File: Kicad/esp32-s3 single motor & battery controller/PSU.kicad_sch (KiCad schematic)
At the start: 67 parts, among them J5 Batt Balance connector, Q1 NMOS, Q2 NMOS, Q3 NMOS, Q4 NMOS, Q5 NMOS, Q6 NMOS, U1 AP2112K-3.3, U3 BQ76905RGRR, U4 BQ24780SRUYR

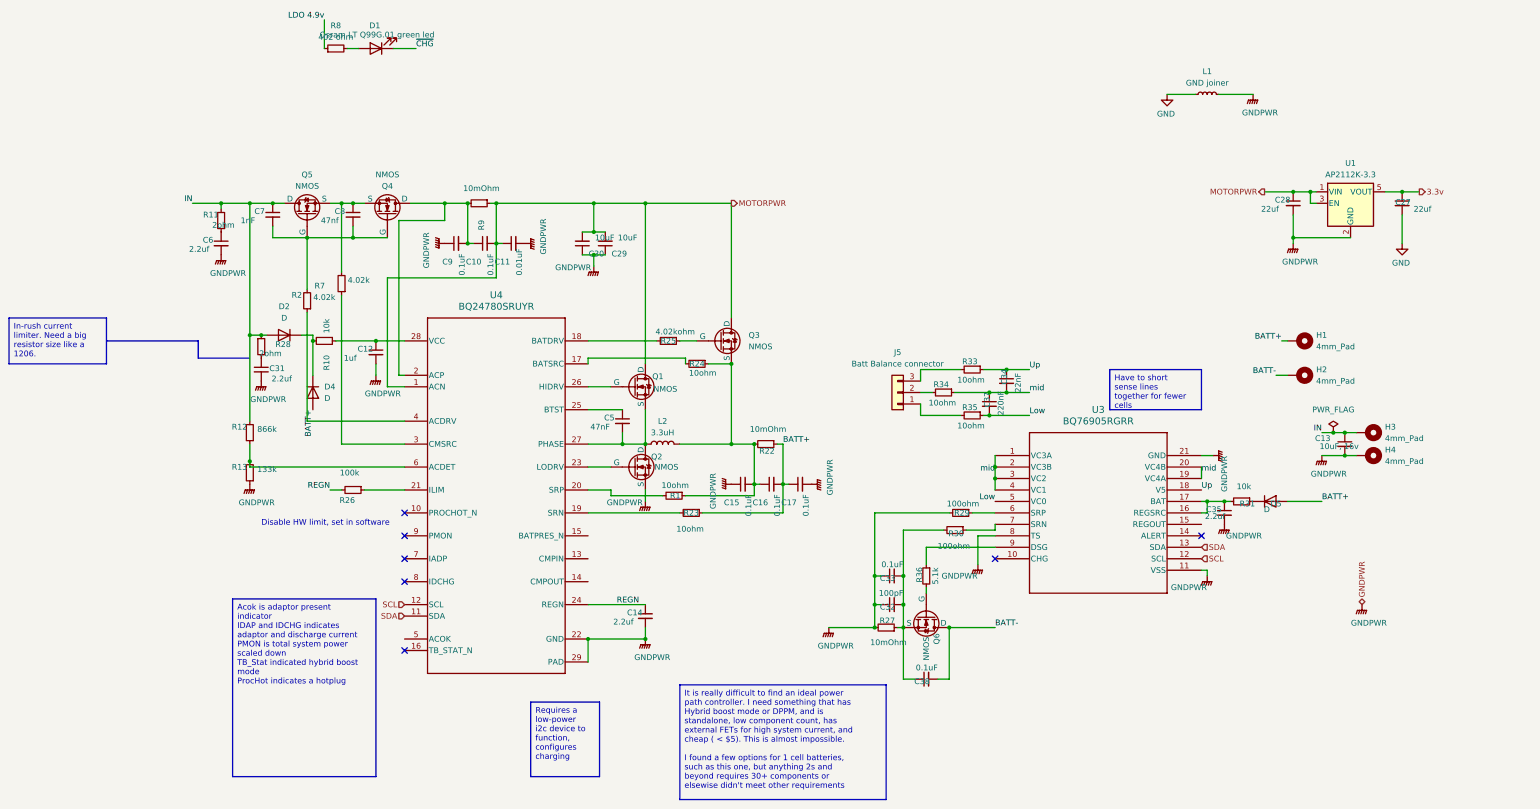
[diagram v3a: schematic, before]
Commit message: Finished schematic routing, Sizing Inductors and mosfets
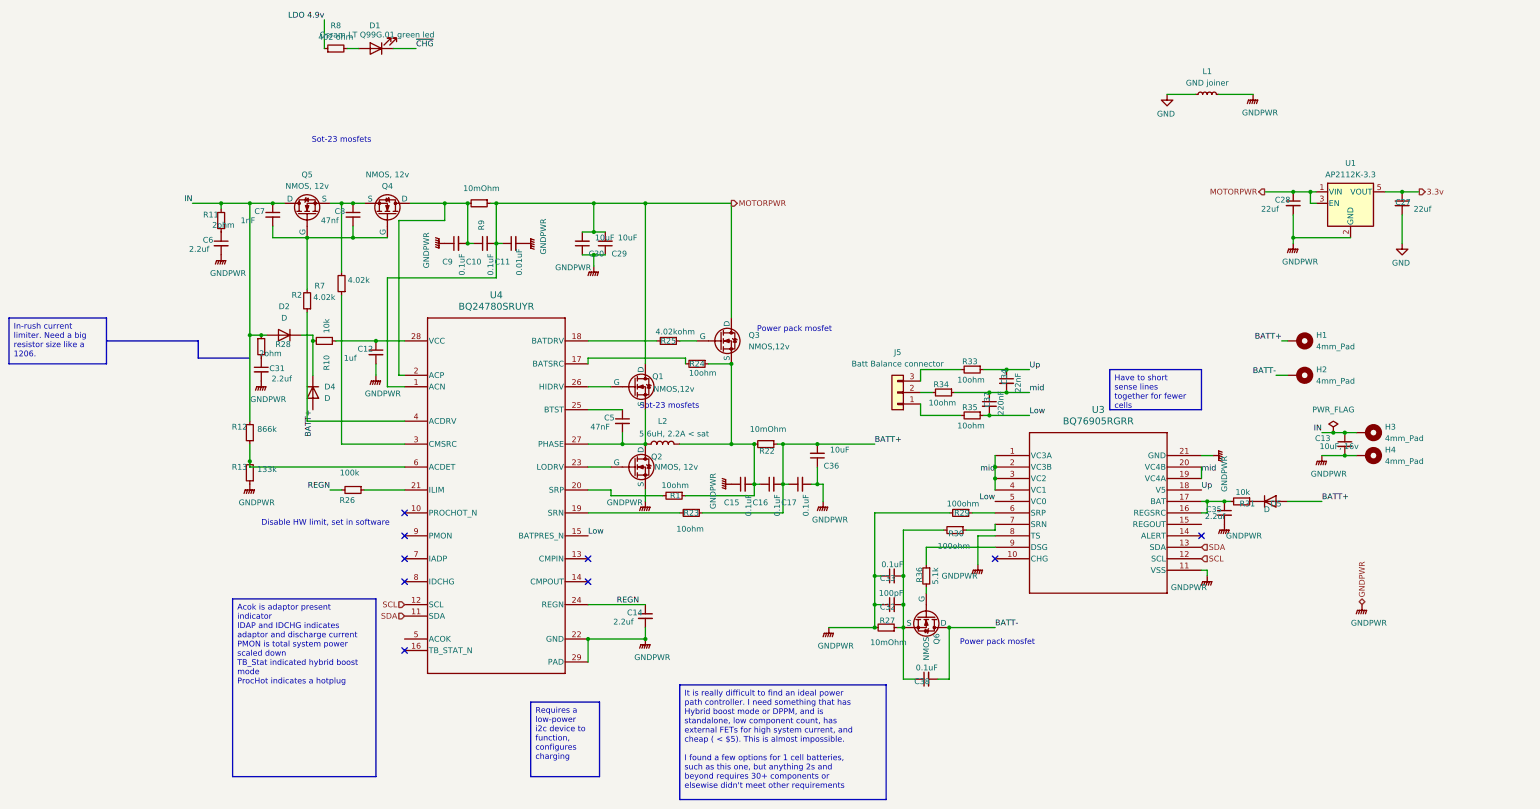
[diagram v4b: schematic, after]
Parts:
- added C36: 10uF, Capacitor_SMD:C_0603_1608Metric, symbol Device:C_Small
- L2: value 3.3uH -> 5.6uH, 2.2A < sat
- Q1, Q3: value NMOS -> NMOS,12v
- Q2, Q4, Q5: value NMOS -> NMOS, 12v
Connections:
- net BATT+: now also C36.2
- net GNDPWR: now also C36.1
- net Low: now also U4.15 (BATPRES_N)
- no-connect marks 7 -> 9
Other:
- note added: "Power pack mosfet"
- note added: "Sot-23 mosfets"
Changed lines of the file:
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@@
 	)
 	(junction
+		(at 144.78 127)
+		(diameter 0)
+		(color 0 0 0 0)
+	)
+	(junction
 		(at 125.73 118.11)
 		(diameter 0)
@@
 	)
 	(junction
+		(at 144.78 118.11)
+		(diameter 0)
+		(color 0 0 0 0)
+	)
+	(junction
 		(at 67.31 64.77)
 		(diameter 0)
@@
 	)
 	(junction
+		(at 137.16 118.11)
+		(diameter 0)
+		(color 0 0 0 0)
+	)
+	(junction
 		(at 261.62 115.57)
 		(diameter 0)
@@
 	)
 	(no_connect
+		(at 93.98 143.51)
+	)
+	(no_connect
 		(at 53.34 148.59)
 	)
 	(no_connect
+		(at 93.98 148.59)
+	)
+	(no_connect
 		(at 184.15 143.51)
 	)
@@
 	(wire
 		(pts
+			(xy 144.78 123.19) (xy 144.78 127)
+		)
+		(stroke
+			(width 0)
+			(type default)
+		)
+	)
+	(wire
+		(pts
 			(xy 233.68 40.64) (xy 241.3 40.64)
 		)
@@
 	(wire
 		(pts
+			(xy 146.05 130.81) (xy 146.05 127)
+		)
+		(stroke
+			(width 0)
+			(type default)
+		)
+	)
+	(wire
+		(pts
 			(xy 93.98 133.35) (xy 114.3 133.35)
 		)
@@
 	(wire
 		(pts
+			(xy 144.78 127) (xy 143.51 127)
+		)
+		(stroke
+			(width 0)
+			(type default)
+		)
+	)
+	(wire
+		(pts
 			(xy 180.34 138.43) (xy 184.15 138.43)
 		)
@@
 	(wire
 		(pts
+			(xy 146.05 127) (xy 144.78 127)
+		)
+		(stroke
+			(width 0)
+			(type default)
+		)
+	)
+	(wire
+		(pts
 			(xy 106.68 110.49) (xy 106.68 118.11)
 		)
@@
 	(wire
 		(pts
+			(xy 144.78 118.11) (xy 157.48 118.11)
+		)
+		(stroke
+			(width 0)
+			(type default)
+		)
+	)
+	(wire
+		(pts
 			(xy 93.98 110.49) (xy 101.6 110.49)
 		)
@@
 	(wire
 		(pts
+			(xy 137.16 118.11) (xy 144.78 118.11)
+		)
+		(stroke
+			(width 0)
+			(type default)
+		)
+	)
+	(wire
+		(pts
 			(xy 261.62 120.65) (xy 264.16 120.65)
 		)
@@
 		)
 	)
+	(text "Sot-23 mosfets"
+		(exclude_from_sim no)
+		(at 39.37 50.8 0)
+		(effects
+			(font
+				(size 1.27 1.27)
+			)
+		)
+	)
+	(text "Sot-23 mosfets"
+		(exclude_from_sim no)
+		(at 112.014 109.728 0)
+		(effects
+			(font
+				(size 1.27 1.27)
+			)
+		)
+	)
 	(text "Disable HW limit, set in software"
 		(exclude_from_sim no)
@@
 		)
 	)
+	(text "Power pack mosfet"
+		(exclude_from_sim no)
+		(at 184.658 162.052 0)
+		(effects
+			(font
+				(size 1.27 1.27)
+			)
+		)
+	)
+	(text "Power pack mosfet"
+		(exclude_from_sim no)
+		(at 139.7 92.71 0)
+		(effects
+			(font
+				(size 1.27 1.27)
+			)
+		)
+	)
 	(label "BATT-"
 		(at 246.38 102.87 180)
@@
 		)
 	)
+	(label "Low"
+		(at 93.98 138.43 0)
+		(fields_autoplaced yes)
+		(effects
+			(font
+				(size 1.27 1.27)
+			)
+			(justify left bottom)
+		)
+	)
 	(label "REGN"
 		(at 36.83 128.27 180)
@@
 	)
 	(label "BATT+"
-		(at 137.16 118.11 0)
+		(at 157.48 118.11 0)
 		(fields_autoplaced yes)
 		(effects
@@
 	)
 	(symbol
+		(lib_id "Device:C_Small")
+		(at 144.78 120.65 180)
+		(unit 1)
+		(exclude_from_sim no)
+		(in_bom yes)
+		(on_board yes)
+		(dnp no)
+		(property "Reference" "C36"
+			(at 149.606 122.936 0)
+			(effects
+				(font
+					(size 1.27 1.27)
+				)
+				(justify left)
+			)
+		)
+		(property "Value" "10uF"
+			(at 151.892 119.38 0)
+			(effects
+				(font
+					(size 1.27 1.27)
+				)
+				(justify left)
+			)
+		)
+		(property "Footprint" "Capacitor_SMD:C_0603_1608Metric"
+			(at 144.78 120.65 0)
+			(effects
+				(font
+					(size 1.27 1.27)
+				)
+				(hide yes)
+			)
+		)
+		(property "Datasheet" "~"
+			(at 144.78 120.65 0)
+			(effects
+				(font
+					(size 1.27 1.27)
+				)
+				(hide yes)
+			)
+		)
+		(property "Description" "Unpolarized capacitor, small symbol"
+			(at 144.78 120.65 0)
+			(effects
+				(font
+					(size 1.27 1.27)
+				)
+				(hide yes)
+			)
+		)
+		(pin "1"
+		)
+		(pin "2"
+		)
+		(instances
+			(project "esp32-s3 single motor & battery controller"
+				(path "/eb3f183d-8bb1-43a5-a363-092ed67891e3/a57a0b4f-e246-497c-8d94-688647d8fd03"
+					(reference "C36")
+					(unit 1)
+				)
+			)
+		)
+	)
+	(symbol
 		(lib_id "power:GNDPWR")
 		(at 106.68 130.81 0)
@@
 			)
 		)
-		(property "Value" "NMOS"
+		(property "Value" "NMOS, 12v"
 			(at 49.53 58.42 90)
 			(effects
@@
 		)
 		(property "Value" "10k"
-			(at 239.268 127.508 90)
+			(at 239.014 128.778 90)
 			(effects
 				(font
@@
 		(on_board yes)
 		(dnp no)
-		(fields_autoplaced yes)
 		(property "Reference" "L2"
 			(at 110.49 113.03 90)
@@
 			)
 		)
-		(property "Value" "3.3uH"
-			(at 110.49 115.57 90)
+		(property "Value" "5.6uH, 2.2A < sat"
+			(at 113.03 115.824 90)
 			(effects
 				(font
@@
 			)
 		)
-		(property "Value" "NMOS"
+		(property "Value" "NMOS, 12v"
 			(at 108.712 123.19 0)
 			(effects
@@
 			)
 		)
-		(property "Value" "NMOS"
+		(property "Value" "NMOS,12v"
 			(at 129.54 96.5199 0)
 			(effects
@@
 			)
 		)
-		(property "Value" "NMOS"
+		(property "Value" "NMOS, 12v"
 			(at 31.75 60.96 90)
 			(effects
@@
 	(symbol
 		(lib_id "power:GNDPWR")
-		(at 143.51 127 90)
+		(at 146.05 130.81 0)
 		(unit 1)
 		(exclude_from_sim no)
@@
 		(dnp no)
 		(property "Reference" "#PWR041"
-			(at 148.59 127 0)
+			(at 146.05 135.89 0)
 			(effects
 				(font
@@
 		)
 		(property "Value" "GNDPWR"
-			(at 147.574 125.476 0)
+			(at 147.574 134.874 0)
 			(effects
 				(font
@@
 		)
 		(property "Footprint" ""
-			(at 144.78 127 0)
+			(at 146.05 132.08 0)
 			(effects
 				(font
@@
 		)
 		(property "Datasheet" ""
-			(at 144.78 127 0)
+			(at 146.05 132.08 0)
 			(effects
 				(font
@@
 		)
 		(property "Description" "Power symbol creates a global label with name \"GNDPWR\" , global ground"
-			(at 143.51 127 0)
+			(at 146.05 130.81 0)
 			(effects
 				(font
@@
 			)
 		)
-		(property "Value" "NMOS"
+		(property "Value" "NMOS,12v"
 			(at 108.458 105.918 0)
 			(effects

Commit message: Finished PSU schematic, Fixed ERC errors
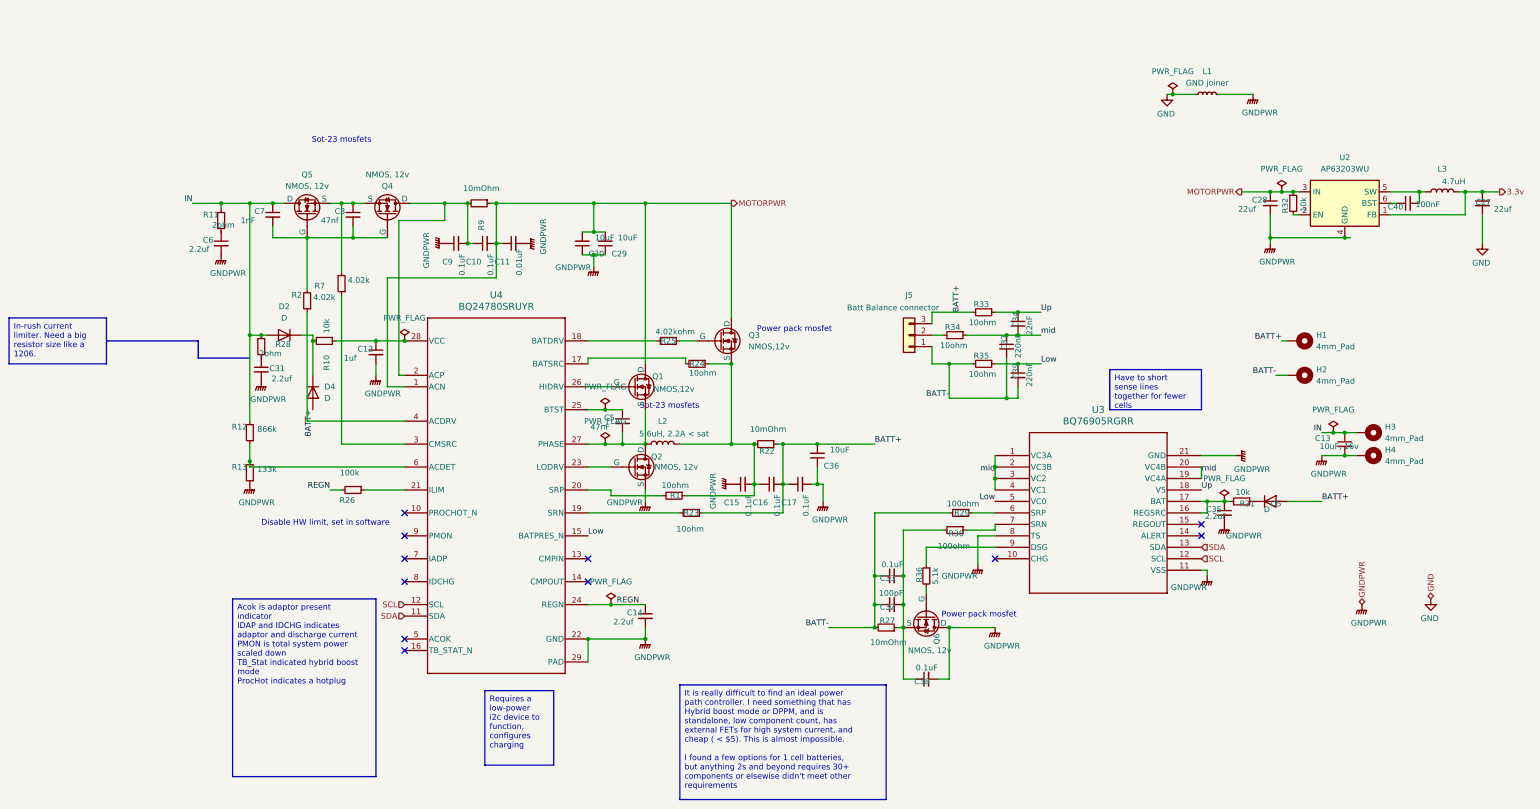
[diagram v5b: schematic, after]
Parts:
- removed D1: Osram LT Q99G.01 green led, LED_SMD:LED_0603_1608Metric_Pad1.05x0.95mm_HandSolder, symbol Device:LED
- removed R8: 402 ohm, Resistor_SMD:R_0603_1608Metric, symbol Device:R_Small
- removed U1: AP2112K-3.3, Package_TO_SOT_SMD:SOT-23-5, symbol Regulator_Linear:AP2112K-3.3
- added C39: 220nF, Capacitor_SMD:C_0603_1608Metric, symbol Device:C_Small
- added C40: 100nF, Capacitor_SMD:C_0603_1608Metric, symbol Device:C_Small
- added L3: 4.7uH, symbol Device:L
- added R32: 10k, Resistor_SMD:R_0603_1608Metric, symbol Device:R_Small
- added U2: AP63203WU, Package_TO_SOT_SMD:TSOT-23-6, symbol Regulator_Switching:AP63203WU
- Q6: value NMOS -> NMOS, 12v
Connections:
- net 3.3v: now also L3.2, U2.1 (FB)
- net BATT+: now also J5.3 (Pin_3), R33.2
- net BATT-: now also C32.1, C33.1, C37.2, J5.1 (Pin_1), R27.2, R29.2, R35.2, C39.2; no longer C38.2, Q6.1 (D)
- net GNDPWR: now also C38.2, Q6.1 (D), U2.4 (GND); no longer C32.1, C33.1, R27.2, R29.2
- net Low: now also C39.1; no longer C37.2
- net MOTORPWR: now also R32.1, U2.3 (IN)
- new net: C40.2, L3.1, U2.5 (SW)
- new net: R32.2, U2.2 (EN)
- new net: C40.1, U2.6 (BST)
- no-connect marks 9 -> 11
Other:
- moved on the sheet: C27, C28, C34, C37, J5, R33, R34, R35
